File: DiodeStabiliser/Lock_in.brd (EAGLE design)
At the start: 101.3 x 78.7 mm, 53 parts, among them IC2 AD712N, IC3 AD712N, IC4 74AC04N

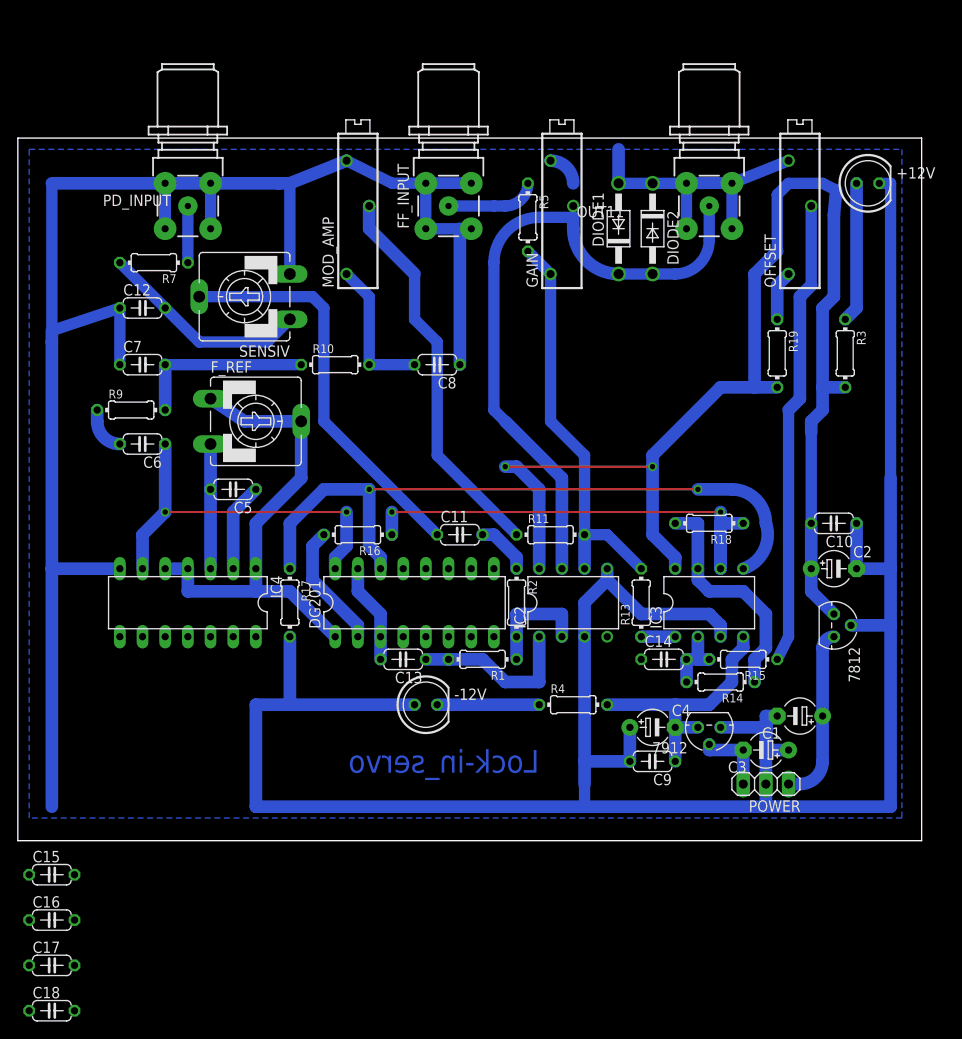
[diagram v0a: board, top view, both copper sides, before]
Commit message: New version of the diode stabliser circuit
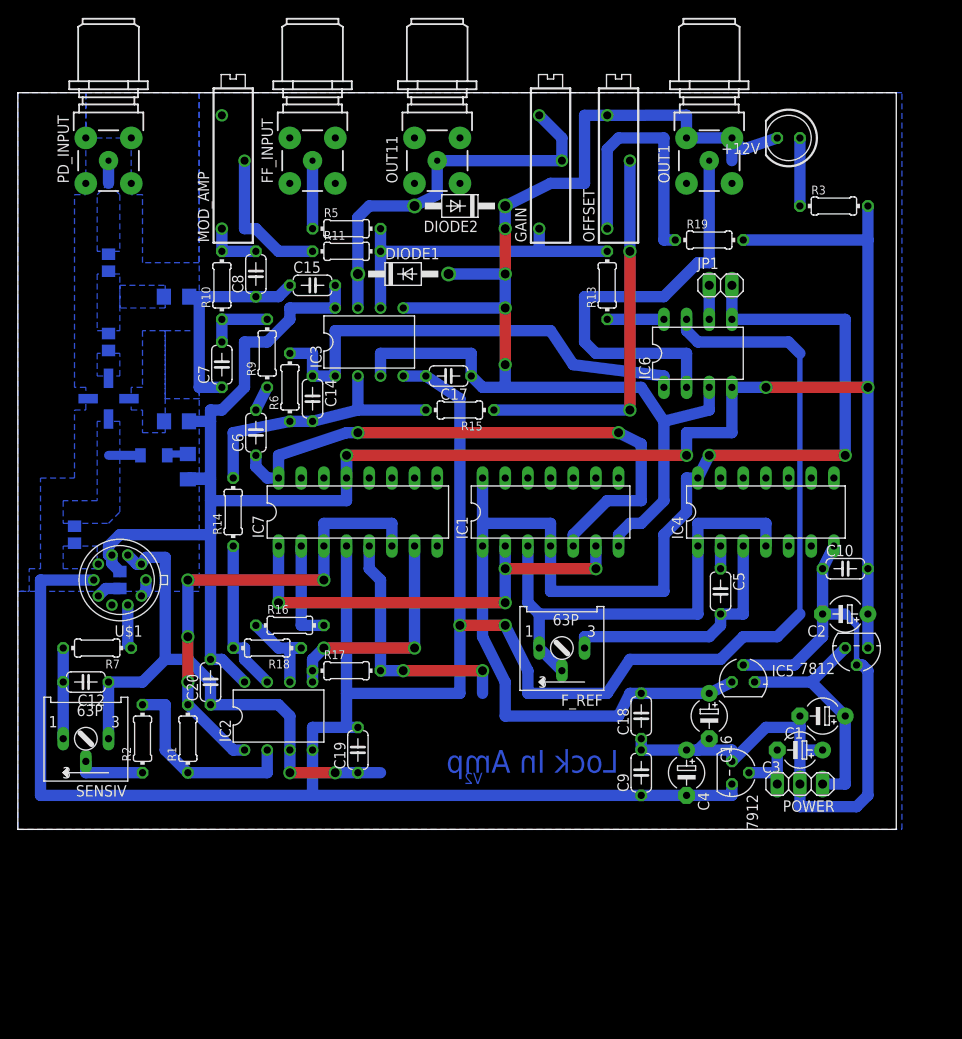
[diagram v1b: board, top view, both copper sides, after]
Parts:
- removed -12V: (no value), led:LED5MM
- removed C11, C13: (no value), rcl:C050-024X044
- removed DG201: dg201, ic-package:DIL16
- added C19, C20: 0.1u, rcl:C050-024X044
- added C21, C22, C24: 0.1u, rcl:C0805
- added C23: 10u, rcl:C1206
- added C25: 1u, rcl:C0805
- added IC1: 74LS74N, 74xx-eu:DIL14
- added IC5: 78L05ACP +5V reg, v-reg:78LXX
- added IC6: DG419CJ, maxim:DIL08
- added IC7: DG201ACJ, maxim:DIL16
- added JP1: (no value), pinhead:1X02
- added L1: 0.22uH, rcl:L3216C
- added OUT1: LEMO00, con-coax:LEMOPAC.PAC
- added R6: 22k, rcl:0204/7
- added R8: 10K, rcl:R1206
- added U$1: AD636, analog-devices:TO100
- added U1: MAR4, custom_parts:VV105
- C1, C2, C3, C4: value 100.0x20 -> 22u
- C10, C14, C15, C17, C18, C9: value (none) -> 0.1u
- C12: value (none) -> 10n
- C16: value (none) -> 22u; device rcl:C050-024X044 -> rcl:E5-4
- C5: value (none) -> 50n
- C6, C7, C8: value (none) -> 1u
- F_REF: value (none) -> 1M; device pot:CA9V -> pot:S63P
- GAIN: value (none) -> 100k
- MOD_AMP, OFFSET: value (none) -> 10k
- R1: value 22k -> 10M
- R10, R9: value 22k -> 10k
- R11, R13, R15, R16, R17, R18, R19, R2, R5: value 22k -> 100k
- R14: value 22k -> 1M
- R3, R7: value 22k -> 1k
- R4: value 22k -> 226; device rcl:0204/7 -> rcl:R1206
- SENSIV: value (none) -> 100k; device pot:CA9V -> pot:S63P
- moved C17 79.6 mm to (48.3, 50.8), turned to 180 degrees
- moved C16 77.1 mm to (77.5, 12.7), turned to 270 degrees
- moved C18 73.8 mm to (69.8, 12.7), turned to 90 degrees
- moved C15 72.2 mm to (33.0, 61.0)
- moved IC4 65.6 mm to (83.8, 35.6), turned to 0 degrees
- moved R14 57.8 mm to (24.1, 35.6), turned to 90 degrees
- moved C5 55.8 mm to (78.7, 26.7), turned to 270 degrees
- moved SENSIV 52.6 mm to (7.62, 10.2), turned to 180 degrees
- moved R18 51.5 mm to (27.9, 20.3)
- moved R4 50.8 mm to (19.1, 40.6), flipped to the bottom, turned to 270 degrees
- moved C14 49.0 mm to (33.0, 48.3), turned to 270 degrees
- moved IC3 48.0 mm to (39.4, 54.6)
- moved R2 44.6 mm to (14.0, 10.2), turned to 90 degrees
- moved R7 43.6 mm to (8.89, 20.3)
- moved F_REF 42.7 mm to (61.0, 20.3), turned to 180 degrees
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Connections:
- removed net F1: DG201.1, F_REF.A, F_REF.S, IC4.1, IC4.4, IC4.5
- removed net N$17: DIODE1.C, DIODE2.A, GAIN.2, GAIN.3, IC2.7, OUT11.1
- removed net N$7: C11.2, R2.1
- removed net N$8: C11.1, SENSIV.S
- new net CLK: F_REF.A, F_REF.S, IC1.3, IC4.1, IC4.4
- new net GND1: IC6.6, JP1.1
- new net N$19: IC6.8, R13.1
- new net N$27: C21.2, U1.RFIN
- new net N$28: C14.1, IC3.1, IC6.1, R6.2
- new net N$29: L1.1, R4.1
- new net N$30: C22.1, L1.2, U1.RFOUT
- new net N$32: C24.2, PD_INPUT.1
- new net N$33: C21.1, C24.1, R8.1
- new net N$34: C22.2, U$1.4
- new net N$35: IC6.2, OUT1.1
- new net N$37: U$1.10, U$1.9
- new net N$38: C25.1, U$1.6
- net F2: now also IC1.5, IC7.16; no longer DG201.16, IC4.6
- net GND: now also C15.1, C16.-, C17.1, C18.1, C19.1, C20.1, C23.2, IC1.7, IC3.5, IC5.GND, IC6.3, IC7.5, OUT1.2, OUT1.3, OUT1.4, OUT1.5, R8.2, U$1.1, U$1.2, U1.GND1, U1.GND2; no longer -12V.A, IC2.5
- net N$10: now also U$1.8; no longer PD_INPUT.1
- net N$14: now also IC3.6; no longer IC2.6
- net N$16: now also IC2.1, IC7.3, IC7.6, R1.2; no longer C13.2, DG201.15, DG201.3
- net N$20: now also IC1.2, IC1.6, IC7.1; no longer C14.1, IC3.1, R13.1
- net N$21: now also R6.1
- net N$22: now also IC7.2; no longer DG201.2
- net N$23: now also IC2.5, IC7.7; no longer DG201.14, IC3.5
- net N$24: now also IC2.6; no longer IC3.6
- net N$25: now also IC2.7; no longer IC3.7
- net N$3: now also DIODE1.C, DIODE2.A, GAIN.2, GAIN.3, IC3.7, OUT11.1; no longer -12V.K, R4.1
- net N$6: now also R2.1, SENSIV.S; no longer C13.1, IC2.1, R1.2
- net V+: now also C15.2, C20.2, C23.1, C25.2, IC6.4, IC7.13, R4.2, U$1.3
- net V+INPUT: now also IC5.IN
- net V-: now also C17.2, C19.2, IC6.7, IC7.4, U$1.5; no longer R4.2
- net VCC: now also C16.+, C18.2, IC1.1, IC1.14, IC1.4, IC5.OUT, IC6.5, JP1.2
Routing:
- net V-: track 29.5 -> 286.9 mm, vias 0 -> 2
- net GND: track 516.3 -> 354.1 mm, vias 0 -> 8
- net VCC: track 0.00 -> 147.3 mm, vias 0 -> 2
- net V+: track 143.2 -> 233.1 mm, vias 2 -> 4
- net N$17: track 76.0 -> 0.00 mm
- net F1: track 55.8 -> 0.00 mm
- net CLK: track 0.00 -> 53.6 mm
- net N$28: track 0.00 -> 52.9 mm
- net N$23: track 76.7 -> 25.9 mm
- net N$35: track 0.00 -> 47.8 mm
- net N$20: track 3.81 -> 50.8 mm, vias 0 -> 4
- net N$8: track 45.2 -> 0.00 mm
- net N$16: track 11.2 -> 54.2 mm, vias 0 -> 4
- net N$24: track 53.3 -> 11.2 mm, vias 2 -> 0
- net N$3: track 11.4 -> 43.8 mm
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- added copper zone on layer 16, net N$27
- added copper zone on layer 16, net N$30
- added copper zone on layer 16, net N$32
- added copper zone on layer 16, net N$33
- added copper zone on layer 16, net N$34
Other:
- board size 101.3 x 78.7 mm -> 98.4 x 82.5 mm
- board text added: "Lock In Amp"
- board text added: "V2"
- board text removed: "Lock-in_servo"
